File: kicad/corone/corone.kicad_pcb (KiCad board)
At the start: 2 copper layers, 63.3 x 49.8 mm, 0 parts

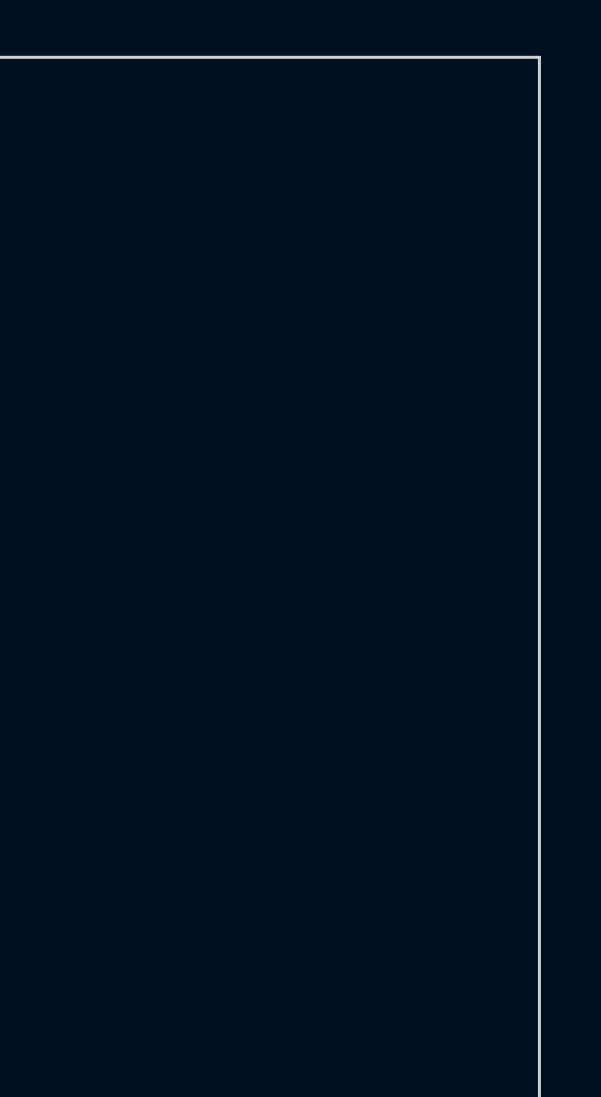
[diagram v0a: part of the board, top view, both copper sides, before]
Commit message: Corone in Moirae's 3D view: J1 placed, mated to J121
Corone's J1 (2x10 socket) goes on its board now, on B, linked to its
schematic symbol so Update PCB keeps it; its 20 pads sit on J121's, mirrored.
tools/export_corone_step.sh exports Corone; COR1, a board-only footprint on
the main board, carries it turned over, its J1 side 12.6 mm behind the main
board's front (J121's 2.5 mm base, the 8.5 mm socket). place_panel_parts.py
keeps COR1 in place. Rerun the export as Corone's layout grows.

Co-Authored-By: Claude Opus 5.5 <noreply@anthropic.com>
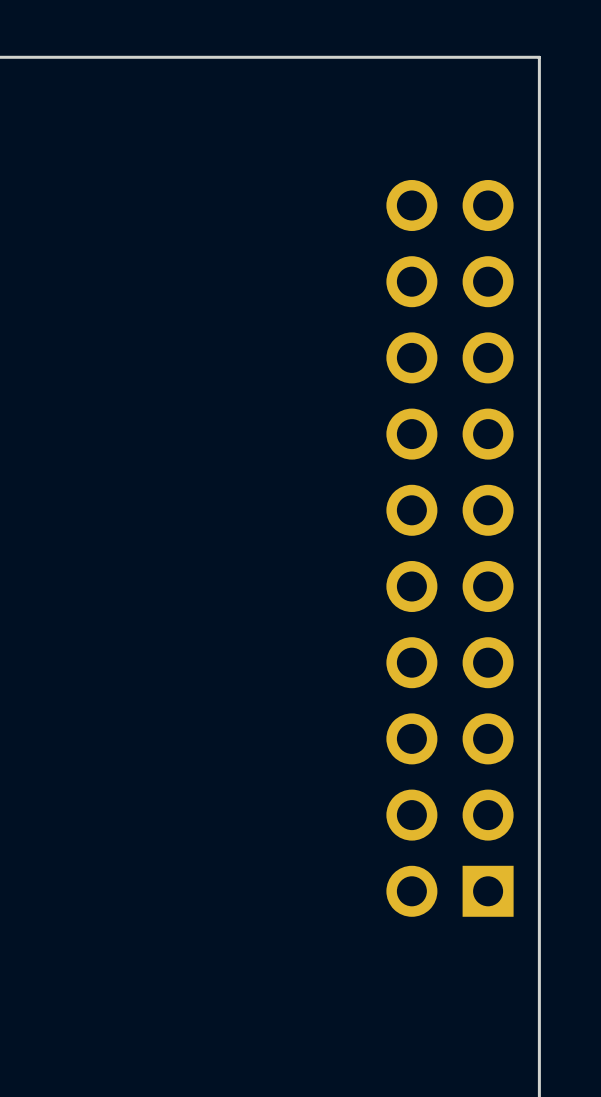
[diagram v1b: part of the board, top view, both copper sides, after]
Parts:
- added J1: To main board, Connector_PinSocket_2.54mm:PinSocket_2x10_P2.54mm_Vertical, B.Cu at (163.3, 126.3)

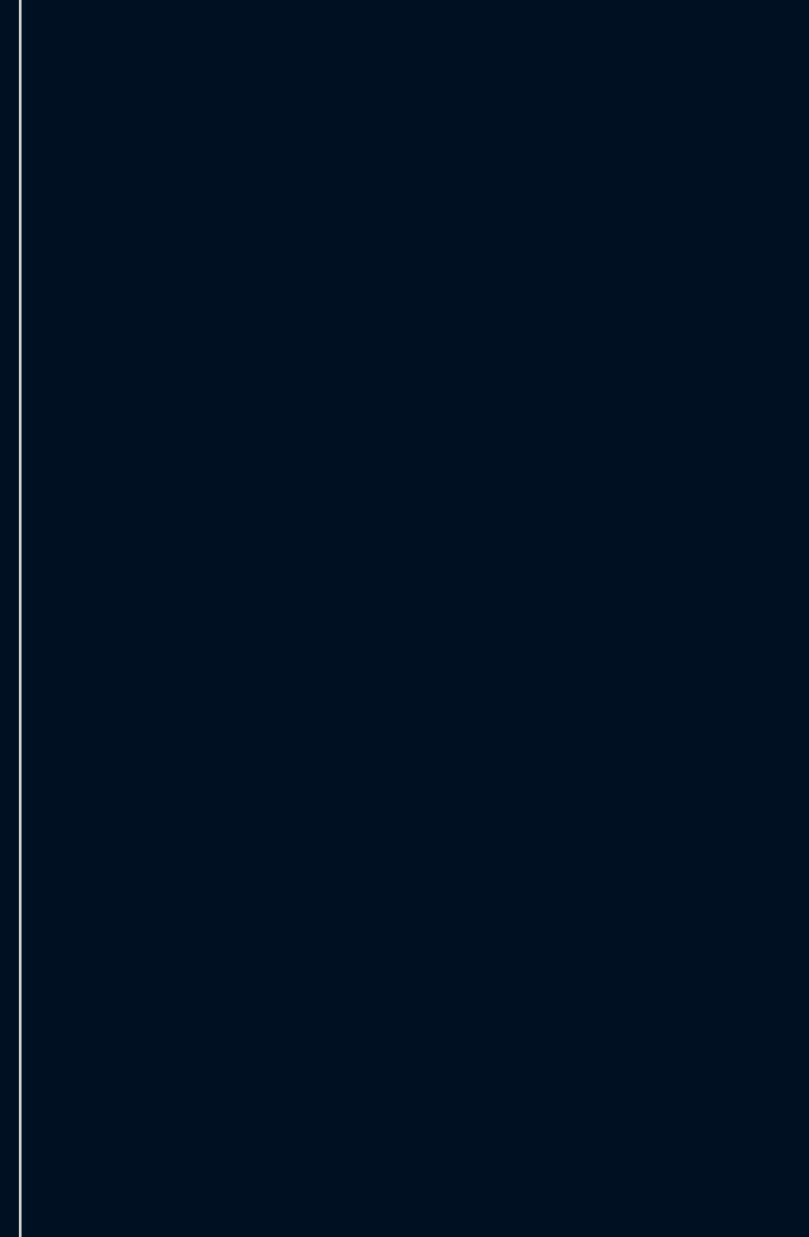
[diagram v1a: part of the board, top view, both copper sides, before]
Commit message: Corone mounting: two M3 holes on both boards
The main board's two M3 holes for Corone's standoffs, at (150.95, 109.9) and
(150.55, 137.0), projected onto Corone as H1 / H2 (MountingHole_3.2mm_M3,
board-only) at (115.70, 109.9) and (116.10, 137.0) in its mirrored frame.
Corone's 3D model re-exported.

Co-Authored-By: Claude Opus 5.5 <noreply@anthropic.com>
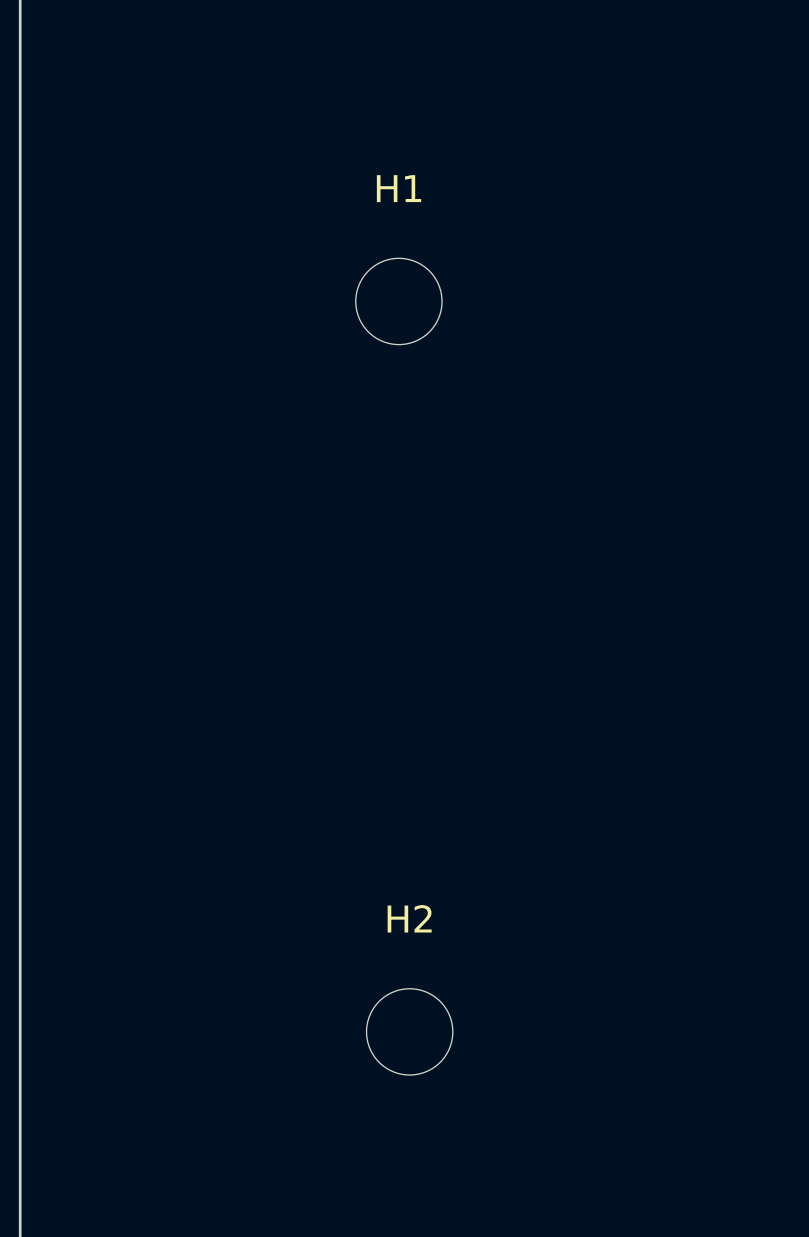
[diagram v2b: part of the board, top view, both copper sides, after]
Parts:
- added H1: M3, MountingHole:MountingHole_3.2mm_M3, F.Cu at (115.7, 109.9)
- added H2: M3, MountingHole:MountingHole_3.2mm_M3, F.Cu at (116.1, 137.0)
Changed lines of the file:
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@@
 		)
+	)
+	(footprint "MountingHole:MountingHole_3.2mm_M3"
+		(locked yes)
+		(layer "F.Cu")
+		(at 115.699999 109.9)
+		(descr "Mounting Hole 3.2mm, M3, no annular, generated by kicad-footprint-generator mountinghole.py")
+		(tags "mountinghole M3")
+		(property "Reference" "H1"
+			(at 0 -4.15 0)
+			(layer "F.SilkS")
+			(effects
+				(font
+					(size 1 1)
+					(thickness 0.15)
+				)
+			)
+		)
+		(property "Value" "M3"
+			(at 0 4.15 0)
+			(layer "F.Fab")
+			(effects
+				(font
+					(size 1 1)
+					(thickness 0.15)
+				)
+			)
+		)
+		(property "Datasheet" ""
+			(at 0 0 0)
+			(layer "F.Fab")
+			(hide yes)
+			(effects
+				(font
+					(size 1.27 1.27)
+				)
+			)
+		)
+		(property "Description" ""
+			(at 0 0 0)
+			(layer "F.Fab")
+			(hide yes)
+			(effects
+				(font
+					(size 1.27 1.27)
+				)
+			)
+		)
+		(property "KiLib_Generator" "mounting_hardware/mounting_hole"
+			(at 0 0 0)
+			(layer "F.SilkS")
+			(hide yes)
+			(effects
+				(font
+					(size 1 1)
+					(thickness 0.15)
+				)
+			)
+		)
+		(attr board_only exclude_from_pos_files exclude_from_bom)
+		(duplicate_pad_numbers_are_jumpers no)
+		(fp_circle
+			(center 0 0)
+			(end 3.2 0)
+			(stroke
+				(width 0.15)
+				(type solid)
+			)
+			(fill no)
+			(layer "Cmts.User")
+		)
+		(fp_circle
+			(center 0 0)
+			(end 3.45 0)
+			(stroke
+				(width 0.05)
+				(type solid)
+			)
+			(fill no)
+			(layer "F.CrtYd")
+		)
+		(fp_text user "${REFERENCE}"
+			(at 0 0 0)
+			(layer "F.Fab")
+			(effects
+				(font
+					(size 1 1)
+					(thickness 0.15)
+				)
+			)
+		)
+		(pad "" np_thru_hole circle
+			(at 0 0)
+			(size 3.2 3.2)
+			(drill 3.2)
+			(layers "*.Cu" "*.Mask")
+		)
+		(embedded_fonts no)
+	)
+	(footprint "MountingHole:MountingHole_3.2mm_M3"
+		(locked yes)
+		(layer "F.Cu")
+		(at 116.099999 137)
+		(descr "Mounting Hole 3.2mm, M3, no annular, generated by kicad-footprint-generator mountinghole.py")
+		(tags "mountinghole M3")
+		(property "Reference" "H2"
+			(at 0 -4.15 0)
+			(layer "F.SilkS")
+			(effects
+				(font
+					(size 1 1)
+					(thickness 0.15)
+				)
+			)
+		)
+		(property "Value" "M3"
+			(at 0 4.15 0)
+			(layer "F.Fab")
+			(effects
+				(font
+					(size 1 1)
+					(thickness 0.15)
+				)
+			)
+		)
+		(property "Datasheet" ""
+			(at 0 0 0)
+			(layer "F.Fab")
+			(hide yes)
+			(effects
+				(font
+					(size 1.27 1.27)
+				)
+			)
+		)
+		(property "Description" ""
+			(at 0 0 0)
+			(layer "F.Fab")
+			(hide yes)
+			(effects
+				(font
+					(size 1.27 1.27)
+				)
+			)
+		)
+		(property "KiLib_Generator" "mounting_hardware/mounting_hole"
+			(at 0 0 0)
+			(layer "F.SilkS")
+			(hide yes)
+			(effects
+				(font
+					(size 1 1)
+					(thickness 0.15)
+				)
+			)
+		)
+		(attr board_only exclude_from_pos_files exclude_from_bom)
+		(duplicate_pad_numbers_are_jumpers no)
+		(fp_circle
+			(center 0 0)
+			(end 3.2 0)
+			(stroke
+				(width 0.15)
+				(type solid)
+			)
+			(fill no)
+			(layer "Cmts.User")
+		)
+		(fp_circle
+			(center 0 0)
+			(end 3.45 0)
+			(stroke
+				(width 0.05)
+				(type solid)
+			)
+			(fill no)
+			(layer "F.CrtYd")
+		)
+		(fp_text user "${REFERENCE}"
+			(at 0 0 0)
+			(layer "F.Fab")
+			(effects
+				(font
+					(size 1 1)
+					(thickness 0.15)
+				)
+			)
+		)
+		(pad "" np_thru_hole circle
+			(at 0 0)
+			(size 3.2 3.2)
+			(drill 3.2)
+			(layers "*.Cu" "*.Mask")
+		)
+		(embedded_fonts no)
 	)
 	(footprint "Connector_PinSocket_2.54mm:PinSocket_2x10_P2.54mm_Vertical"

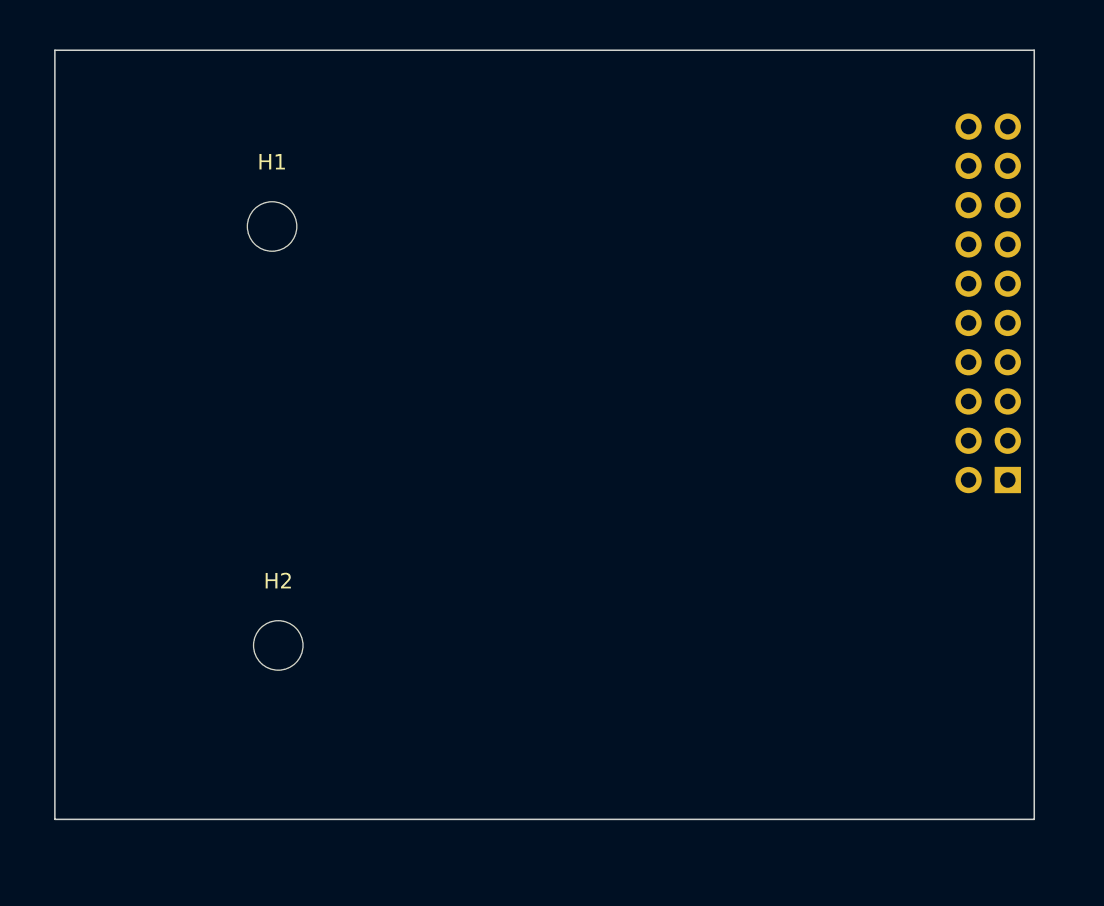
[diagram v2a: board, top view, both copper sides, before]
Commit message: Corone: GND stitching and escape vias
stitch_ground.py takes a board path, so it stitches Corone too: 44 grid
vias, then 12 short stubs and vias for GND pads the pour could not reach.

Co-Authored-By: Claude Opus 5.5 <noreply@anthropic.com>
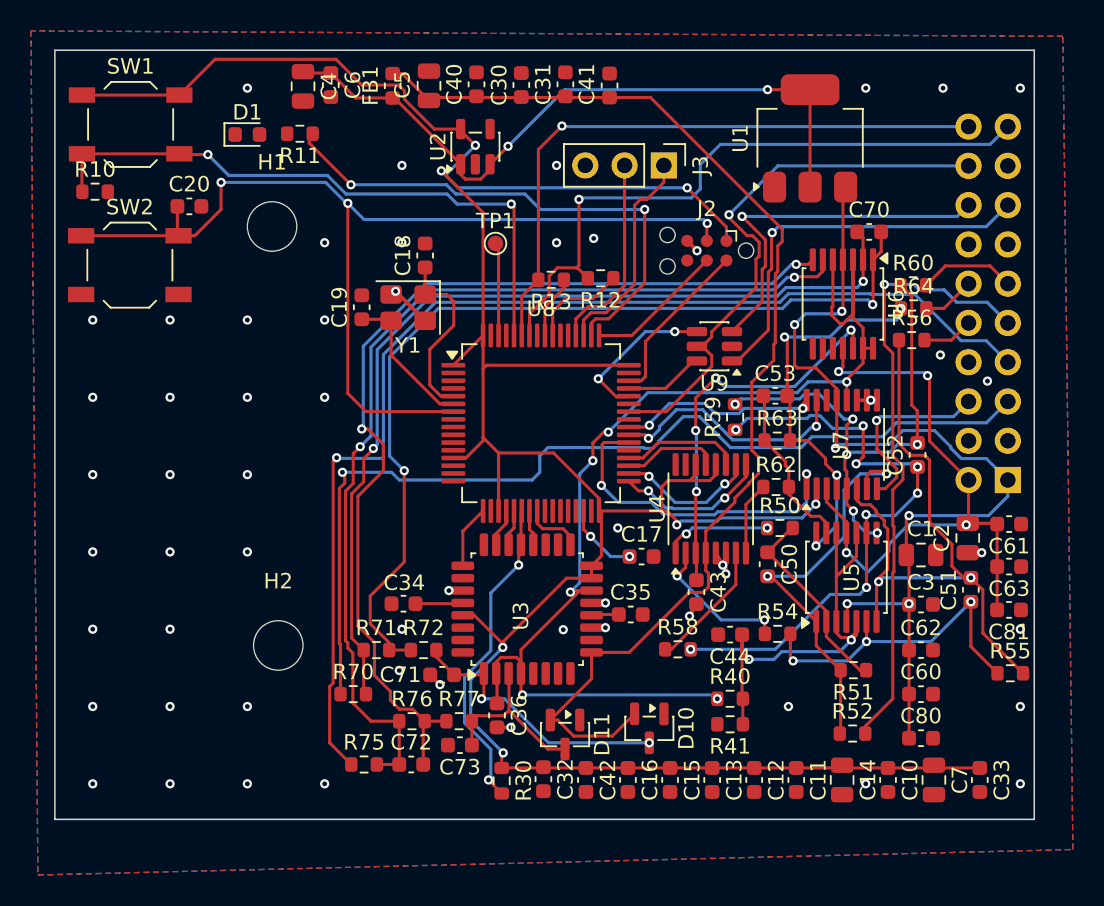
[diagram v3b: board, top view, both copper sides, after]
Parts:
- added C1: 10u 25V, Capacitor_SMD:C_0805_2012Metric, F.Cu at (157.7, 131.2)
- added C10: 100n, Capacitor_SMD:C_0603_1608Metric, F.Cu at (155.5, 145.7)
- added C11: 100n, Capacitor_SMD:C_0603_1608Metric, F.Cu at (149.6, 145.7)
- added C12: 100n, Capacitor_SMD:C_0603_1608Metric, F.Cu at (146.9, 145.7)
- added C13: 100n, Capacitor_SMD:C_0603_1608Metric, F.Cu at (144.2, 145.7)
- added C14: 4u7, Capacitor_SMD:C_0805_2012Metric, F.Cu at (152.6, 145.7)
- added C15: 1u, Capacitor_SMD:C_0603_1608Metric, F.Cu at (141.4, 145.7)
- added C16: 100n, Capacitor_SMD:C_0603_1608Metric, F.Cu at (138.7, 145.7)
- added C17: 2u2, Capacitor_SMD:C_0603_1608Metric, F.Cu at (139.6, 131.2)
- added C18: 12p, Capacitor_SMD:C_0603_1608Metric, F.Cu at (125.6, 111.8)
- added C19: 12p, Capacitor_SMD:C_0603_1608Metric, F.Cu at (121.5, 115.1)
- added C2: 10u 25V, Capacitor_SMD:C_0805_2012Metric, F.Cu at (160.7, 130.1)
- added C20: 100n, Capacitor_SMD:C_0603_1608Metric, F.Cu at (110.3, 108.6)
- added C3: 1u 25V, Capacitor_SMD:C_0603_1608Metric, F.Cu at (157.7, 134.3)
- added C30: 1u, Capacitor_SMD:C_0603_1608Metric, F.Cu at (131.8, 100.7)
- added C31: 100n, Capacitor_SMD:C_0603_1608Metric, F.Cu at (134.7, 100.7)
- added C32: 1u, Capacitor_SMD:C_0603_1608Metric, F.Cu at (133.2, 145.7)
- added C33: 1u, Capacitor_SMD:C_0603_1608Metric, F.Cu at (161.5, 145.7)
- added C34: 1u, Capacitor_SMD:C_0603_1608Metric, F.Cu at (124.2, 134.3)
- added C35: 1u, Capacitor_SMD:C_0603_1608Metric, F.Cu at (138.9, 135.0)
- added C36: 100n, Capacitor_SMD:C_0603_1608Metric, F.Cu at (130.2, 141.5)
- added C4: 10u, Capacitor_SMD:C_0805_2012Metric, F.Cu at (117.7, 100.8)
- added C40: 1u, Capacitor_SMD:C_0603_1608Metric, F.Cu at (128.9, 100.7)
- added C41: 100n, Capacitor_SMD:C_0603_1608Metric, F.Cu at (137.5, 100.8)
- added C42: 100n, Capacitor_SMD:C_0603_1608Metric, F.Cu at (136.0, 145.7)
- added C43: 150n, Capacitor_SMD:C_0603_1608Metric, F.Cu at (143.2, 133.6)
- added C44: 100n, Capacitor_SMD:C_0603_1608Metric, F.Cu at (145.3, 136.3)
- added C5: 10u, Capacitor_SMD:C_0805_2012Metric, F.Cu at (125.8, 100.8)
- added C50: 100p, Capacitor_SMD:C_0603_1608Metric, F.Cu at (147.8, 131.8)
- added C51: 100p, Capacitor_SMD:C_0603_1608Metric, F.Cu at (160.9, 133.4)
- added C52: 100p, Capacitor_SMD:C_0603_1608Metric, F.Cu at (157.4, 124.7)
- added C53: 100p, Capacitor_SMD:C_0603_1608Metric, F.Cu at (148.2, 120.8)
- added C6: 1u, Capacitor_SMD:C_0603_1608Metric, F.Cu at (119.5, 100.8)
- added C60: 100n, Capacitor_SMD:C_0603_1608Metric, F.Cu at (157.7, 140.2)
- added C61: 100n, Capacitor_SMD:C_0603_1608Metric, F.Cu at (163.4, 129.2)
- added C62: 100n, Capacitor_SMD:C_0603_1608Metric, F.Cu at (157.7, 137.3)
- added C63: 100n, Capacitor_SMD:C_0603_1608Metric, F.Cu at (163.4, 131.9)
- added C7: 10u, Capacitor_SMD:C_0805_2012Metric, F.Cu at (158.5, 145.7)
- added C70: 1n, Capacitor_SMD:C_0603_1608Metric, F.Cu at (154.3, 110.2)
- added C71: 1n, Capacitor_SMD:C_0603_1608Metric, F.Cu at (126.7, 138.9)
- added C72: 1n, Capacitor_SMD:C_0603_1608Metric, F.Cu at (124.7, 144.7)
- added C73: 1n, Capacitor_SMD:C_0603_1608Metric, F.Cu at (127.8, 143.4)
- added C80: 100n, Capacitor_SMD:C_0603_1608Metric, F.Cu at (157.7, 143.0)
- added C81: 100n, Capacitor_SMD:C_0603_1608Metric, F.Cu at (163.4, 134.7)
- added D1: status, LED_SMD:LED_0603_1608Metric, F.Cu at (114.1, 104.0)
- added D10: BAT54S, Package_TO_SOT_SMD:SOT-23, F.Cu at (140.1, 142.4)
- added D11: BAT54S, Package_TO_SOT_SMD:SOT-23, F.Cu at (134.7, 142.8)
- added FB1: 600R@100MHz, Inductor_SMD:L_0603_1608Metric, F.Cu at (123.5, 100.8)
- added J2: SWD, Connector:Tag-Connect_TC2030-IDC-NL_2x03_P1.27mm_Vertical, F.Cu at (143.8, 111.5)
- added J3: Debug UART, Connector_PinHeader_2.54mm:PinHeader_1x03_P2.54mm_Vertical, F.Cu at (141.0, 106.0)
- added R10: 10k, Resistor_SMD:R_0603_1608Metric, F.Cu at (104.2, 107.7)
- added R11: 1k, Resistor_SMD:R_0603_1608Metric, F.Cu at (117.5, 103.9)
- added R12: 2.2k, Resistor_SMD:R_0603_1608Metric, F.Cu at (136.9, 113.2)
- added R13: 2.2k, Resistor_SMD:R_0603_1608Metric, F.Cu at (133.8, 113.3)
- added R30: 100k, Resistor_SMD:R_0603_1608Metric, F.Cu at (130.6, 145.8)
- added R40: 30k, Resistor_SMD:R_0603_1608Metric, F.Cu at (145.3, 140.4)
- added R41: 40k, Resistor_SMD:R_0603_1608Metric, F.Cu at (145.3, 142.1)
- added R50: 20k, Resistor_SMD:R_0603_1608Metric, F.Cu at (148.6, 129.4)
- added R51: 120k, Resistor_SMD:R_0603_1608Metric, F.Cu at (153.3, 138.6)
- added R52: 1k, Resistor_SMD:R_0603_1608Metric, F.Cu at (153.2, 142.7)
- added R54: 20k, Resistor_SMD:R_0603_1608Metric, F.Cu at (148.4, 136.2)
- added R55: 120k, Resistor_SMD:R_0603_1608Metric, F.Cu at (163.4, 138.8)
- added R56: 1k, Resistor_SMD:R_0603_1608Metric, F.Cu at (157.1, 117.2)
- added R58: 20k, Resistor_SMD:R_0603_1608Metric, F.Cu at (141.9, 137.2)
- added R59: 120k, Resistor_SMD:R_0603_1608Metric, F.Cu at (145.7, 122.2)
- added R60: 1k, Resistor_SMD:R_0603_1608Metric, F.Cu at (157.2, 113.7)
- added R62: 20k, Resistor_SMD:R_0603_1608Metric, F.Cu at (148.3, 126.8)
- added R63: 120k, Resistor_SMD:R_0603_1608Metric, F.Cu at (148.4, 123.8)
- added R64: 1k, Resistor_SMD:R_0603_1608Metric, F.Cu at (157.2, 115.2)
- added R70: 100k, Resistor_SMD:R_0603_1608Metric, F.Cu at (121.0, 140.2)
- added R71: 33.2k, Resistor_SMD:R_0603_1608Metric, F.Cu at (122.5, 137.3)
- added R72: 1k, Resistor_SMD:R_0603_1608Metric, F.Cu at (125.5, 137.3)
- added R75: 100k, Resistor_SMD:R_0603_1608Metric, F.Cu at (121.7, 144.7)
- added R76: 33.2k, Resistor_SMD:R_0603_1608Metric, F.Cu at (124.8, 141.9)
- added R77: 1k, Resistor_SMD:R_0603_1608Metric, F.Cu at (127.8, 141.9)
- added SW1: BOOT0, Button_Switch_SMD:SW_SPST_TL3342, F.Cu at (106.5, 103.3)
- added SW2: RESET, Button_Switch_SMD:SW_SPST_TL3342, F.Cu at (106.5, 112.4)
- added TP1: DBG_PIN, TestPoint:TestPoint_Pad_D1.0mm, F.Cu at (130.2, 111.0)
- added U1: AMS1117-5.0, Package_TO_SOT_SMD:SOT-223-3_TabPin2, F.Cu at (150.5, 104.2)
- added U2: AP2112K-3.3, Package_TO_SOT_SMD:SOT-23-5, F.Cu at (128.8, 104.7)
- added U3: ADS131A02IPBS, Package_QFP:TQFP-32_7x7mm_P0.8mm, F.Cu at (132.2, 134.7)
- added U4: DAC8565IAPW, Package_SO:TSSOP-16_4.4x5mm_P0.65mm, F.Cu at (144.1, 128.2)
- added U5: OPA4197, Package_SO:TSSOP-14_4.4x5mm_P0.65mm, F.Cu at (152.8, 132.6)
- added U6: OPA4197, Package_SO:TSSOP-14_4.4x5mm_P0.65mm, F.Cu at (152.6, 114.9)
- added U7: ADG1408YRUZ, Package_SO:TSSOP-16_4.4x5mm_P0.65mm, F.Cu at (152.6, 124.0)
- added U8: STM32F722RET6, Package_QFP:LQFP-64_10x10mm_P0.5mm, F.Cu at (133.1, 122.6)
- added U9: USBLC6-2SC6, Package_TO_SOT_SMD:SOT-23-6, F.Cu at (144.3, 117.7)
- added Y1: 8MHz, Crystal:Crystal_SMD_3225-4Pin_3.2x2.5mm, F.Cu at (124.5, 115.2)
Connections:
- J1 pad 1: (no net) -> +12V
- J1 pad 10: (no net) -> /OUT2
- J1 pad 11: (no net) -> /OUT3
- J1 pad 12: (no net) -> /OUT4
- J1 pad 13: (no net) -> GND
- J1 pad 14: (no net) -> GND
- J1 pad 15: (no net) -> /USB_DP_EXT
- J1 pad 16: (no net) -> /USB_DM_EXT
- J1 pad 17: (no net) -> GND
- J1 pad 18: (no net) -> /VBUS
- J1 pad 19: (no net) -> /II_SCL
- J1 pad 2: (no net) -> -12V
- J1 pad 20: (no net) -> /II_SDA
- J1 pad 3: (no net) -> GND
- J1 pad 4: (no net) -> GND
- J1 pad 5: (no net) -> /IN1
- J1 pad 6: (no net) -> /IN1_NORM
- J1 pad 7: (no net) -> /IN2
- J1 pad 8: (no net) -> GND
- J1 pad 9: (no net) -> /OUT1
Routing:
- net +3V3: track 0.00 -> 179.5 mm, vias 0 -> 7
- net /REF_2V5: track 0.00 -> 76.2 mm, vias 0 -> 6
- net +5VA: track 0.00 -> 76.2 mm
- net /IN2: track 0.00 -> 74.2 mm, vias 0 -> 1
- net /NRST: track 0.00 -> 66.6 mm, vias 0 -> 3
- net /ISUM2: track 0.00 -> 63.6 mm, vias 0 -> 2
- net /IAMP2: track 0.00 -> 63.5 mm, vias 0 -> 2
- net /IN1: track 0.00 -> 62.3 mm, vias 0 -> 1
- net +12V: track 0.00 -> 61.3 mm, vias 0 -> 6
- net /IAMP1: track 0.00 -> 60.0 mm, vias 0 -> 2
- net /ISUM1: track 0.00 -> 59.8 mm, vias 0 -> 2
- net +5V: track 0.00 -> 44.4 mm, vias 0 -> 2
- net /II_SCL: track 0.00 -> 42.5 mm, vias 0 -> 1
- net /OAMP2: track 0.00 -> 41.8 mm, vias 0 -> 2
- net -12V: track 0.00 -> 41.2 mm, vias 0 -> 4
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- added copper zone on B.Cu, net GND
- added copper zone on F.Cu, net GND

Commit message: Corone: solid zone connection on starved-thermal GND pads
Co-Authored-By: Claude Opus 5.5 <noreply@anthropic.com>
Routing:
- net GND: track 13.0 -> 20.3 mm, vias 56 -> 58

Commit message: Corone: tie the last GND islands in; 0 unconnected
Vias bond four floating pour pieces to the other layer's plane, and U3
pin 32 gets a stub and via of its own.

Co-Authored-By: Claude Opus 5.5 <noreply@anthropic.com>
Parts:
- moved R63 0.12 mm to (148.3, 123.7)
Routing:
- net GND: track 20.3 -> 85.0 mm, vias 58 -> 81
- net /LED_A: track 0.00 -> 1.81 mm
- net /U6C_OUT: track 0.00 -> 0.65 mm
- net +5V: track 44.4 -> 45.0 mm
- net +12V: track 61.3 -> 60.8 mm
